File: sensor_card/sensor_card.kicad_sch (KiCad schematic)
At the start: 9 parts, among them J1 Raspberry_Pi_4, J2 BME280, J3 GPS, J4 MPU, J5 parachute, J6 hmi, J7 power, U1 Ai-Thinker-Ra-02

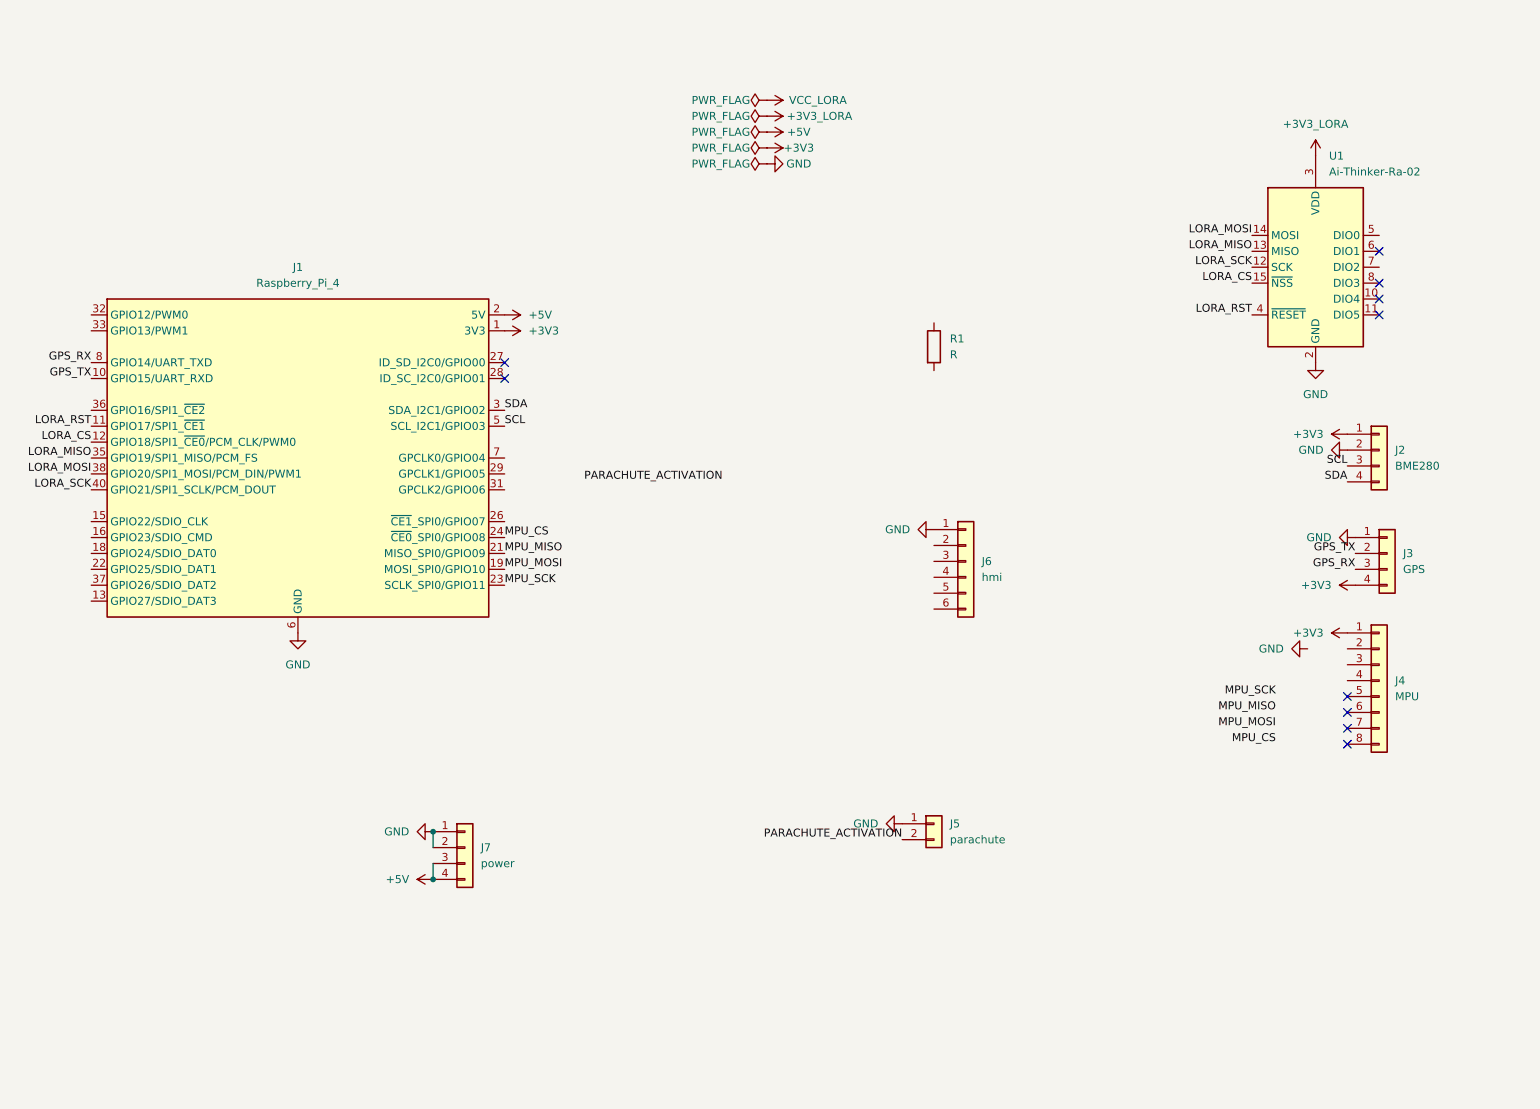
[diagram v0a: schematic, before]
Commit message: Sensor Board Fully Connected
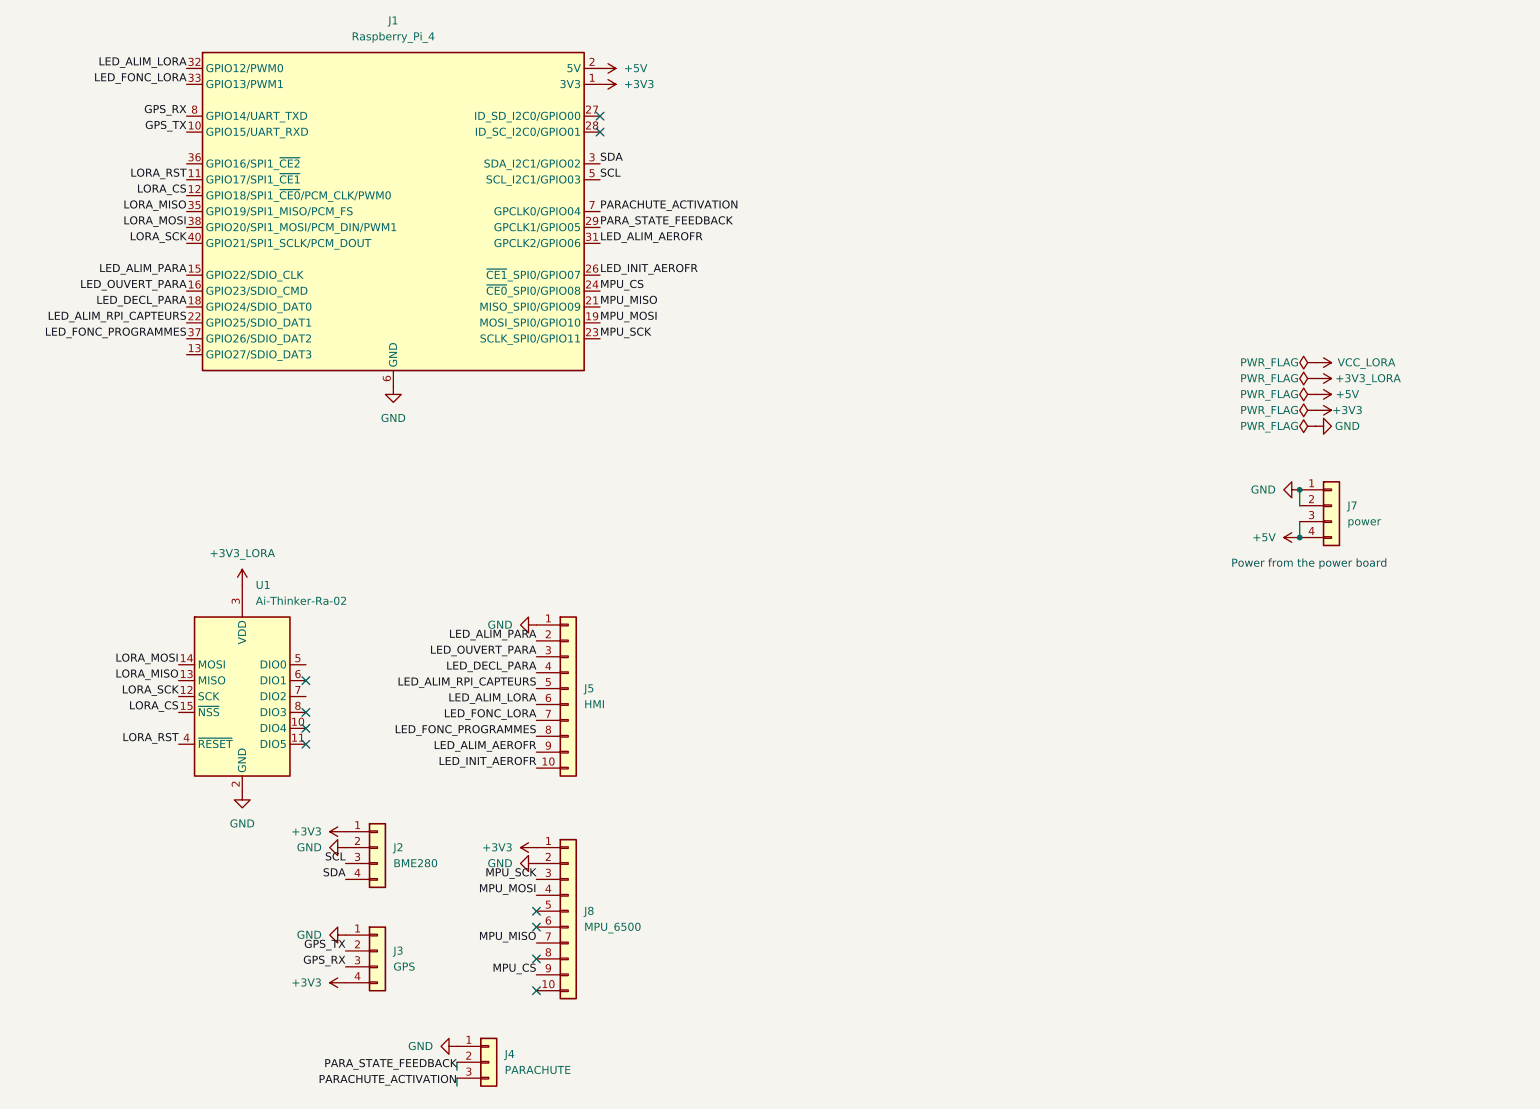
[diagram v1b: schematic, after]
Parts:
- removed J4: MPU, symbol Connector_Generic:Conn_01x08
- removed J5: parachute, symbol Connector_Generic:Conn_01x02
- removed J6: hmi, symbol Connector_Generic:Conn_01x06
- removed R1: R, symbol Device:R
- added J4: PARACHUTE, symbol Connector_Generic:Conn_01x03
- added J5: HMI, symbol Connector_Generic:Conn_01x10
- added J8: MPU_6500, symbol Connector_Generic:Conn_01x10
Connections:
- net +3V3: now also J8.1 (Pin_1)
- net GND: now also J4.1 (Pin_1), J5.1 (Pin_1), J8.2 (Pin_2)
- net MPU_CS: now also J8.9 (Pin_9)
- net MPU_MISO: now also J8.7 (Pin_7)
- net MPU_MOSI: now also J8.4 (Pin_4)
- net MPU_SCK: now also J8.3 (Pin_3)
- net PARACHUTE_ACTIVATION: now also J1.7 (GPCLK0/GPIO04), J4.3 (Pin_3)
- net LED_ALIM_PARA: now reaches J1.15 (GPIO22/SDIO_CLK)
- net LED_ALIM_PARA: now also J5.2 (Pin_2)
- net LED_OUVERT_PARA: now reaches J1.16 (GPIO23/SDIO_CMD)
- net LED_OUVERT_PARA: now also J5.3 (Pin_3)
- net LED_DECL_PARA: now reaches J1.18 (GPIO24/SDIO_DAT0)
- net LED_DECL_PARA: now also J5.4 (Pin_4)
- net LED_ALIM_RPI_CAPTEURS: now reaches J1.22 (GPIO25/SDIO_DAT1)
- net LED_ALIM_RPI_CAPTEURS: now also J5.5 (Pin_5)
- net LED_INIT_AEROFR: now reaches J1.26 (~{CE1}_SPI0/GPIO07)
- net LED_INIT_AEROFR: now also J5.10 (Pin_10)
- net PARA_STATE_FEEDBACK: now reaches J1.29 (GPCLK1/GPIO05)
- net PARA_STATE_FEEDBACK: now also J4.2 (Pin_2)
- net LED_ALIM_AEROFR: now reaches J1.31 (GPCLK2/GPIO06)
- net LED_ALIM_AEROFR: now also J5.9 (Pin_9)
- net LED_ALIM_LORA: now reaches J1.32 (GPIO12/PWM0)
- net LED_ALIM_LORA: now also J5.6 (Pin_6)
- net LED_FONC_LORA: now reaches J1.33 (GPIO13/PWM1)
- net LED_FONC_LORA: now also J5.7 (Pin_7)
- net LED_FONC_PROGRAMMES: now reaches J1.37 (GPIO26/SDIO_DAT2)
- net LED_FONC_PROGRAMMES: now also J5.8 (Pin_8)
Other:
- note added: "Power from the power board"
- moved on the sheet: J1, J2, J3, J7, U1

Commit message: Updated Sensor PCB
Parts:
- added J6: power LORA, Connector_JST:JST_XH_S4B-XH-A-1_1x04_P2.50mm_Horizontal, symbol Connector_Generic:Conn_01x04
- J1: footprint (none) -> Connector_PinHeader_2.54mm:PinHeader_2x20_P2.54mm_Vertical
- J2, J3: footprint (none) -> Connector_PinHeader_2.54mm:PinHeader_1x04_P2.54mm_Vertical
- J4: footprint (none) -> Connector_JST:JST_XH_S3B-XH-A_1x03_P2.50mm_Horizontal
- J5: footprint (none) -> Connector_JST:JST_XH_B10B-XH-A_1x10_P2.50mm_Vertical
- J7: value power -> power_RPI; footprint (none) -> Connector_JST:JST_XH_S4B-XH-A-1_1x04_P2.50mm_Horizontal
- J8: footprint (none) -> Connector_PinHeader_2.54mm:PinHeader_1x10_P2.54mm_Vertical
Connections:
- net +3V3_LORA: now also J6.3 (Pin_3), J6.4 (Pin_4)
- net GND: now also J6.1 (Pin_1), J6.2 (Pin_2)
- no-connect marks 10 -> 14
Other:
- note added: "Power for the LORA"
- note added: "Power from the power board for powering up the RPI"
- note removed: "Power from the power board"
- moved on the sheet: J7

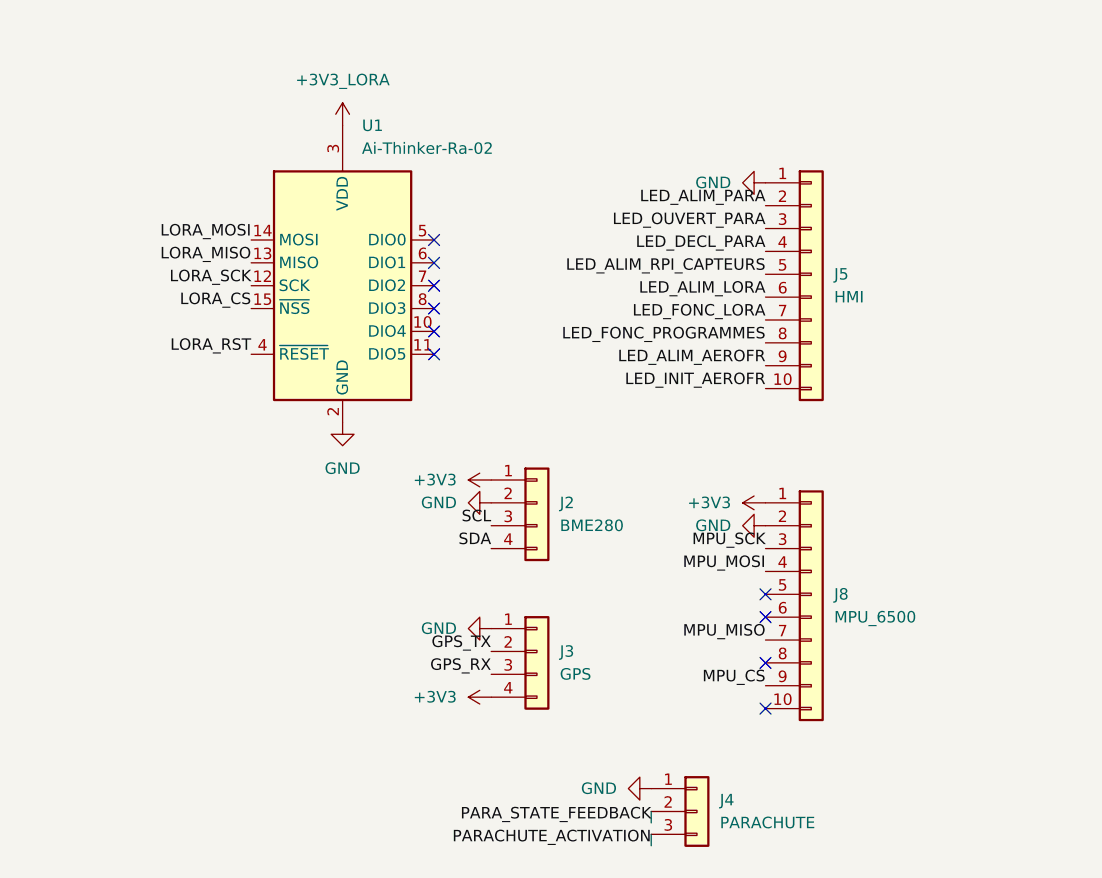
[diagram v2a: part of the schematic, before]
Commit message: Board Routed Prototype 1 .  Power Routes to be redone
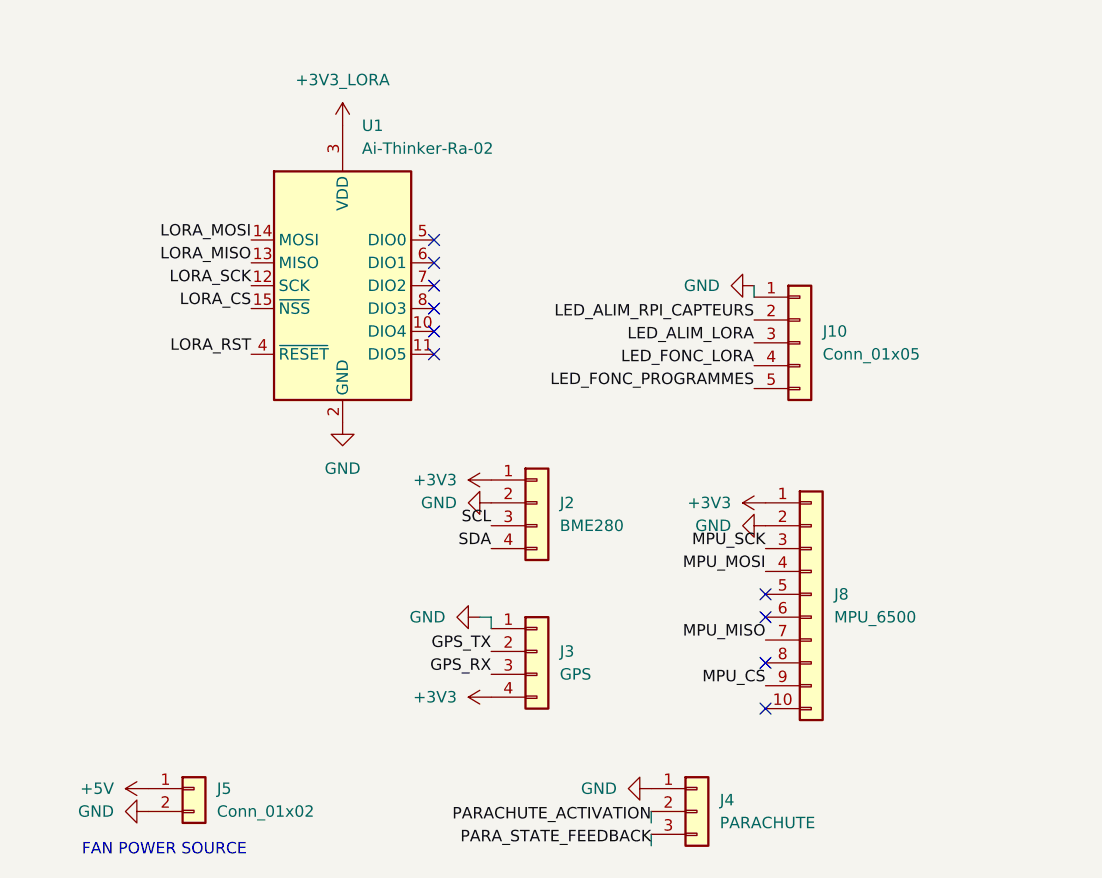
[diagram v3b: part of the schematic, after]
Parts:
- removed J5: HMI, Connector_JST:JST_XH_B10B-XH-A_1x10_P2.50mm_Vertical, symbol Connector_Generic:Conn_01x10
- added J10: Conn_01x05, Connector_JST:JST_XH_S5B-XH-A-1_1x05_P2.50mm_Horizontal, symbol Connector_Generic:Conn_01x05
- added J5: Conn_01x02, Connector_JST:JST_XH_S2B-XH-A_1x02_P2.50mm_Horizontal, symbol Connector_Generic:Conn_01x02
- J2: footprint Connector_PinHeader_2.54mm:PinHeader_1x04_P2.54mm_Vertical -> PHOENIX:BME 280
- J3: footprint Connector_PinHeader_2.54mm:PinHeader_1x04_P2.54mm_Vertical -> PHOENIX:GPS-MV2
- J8: footprint Connector_PinHeader_2.54mm:PinHeader_1x10_P2.54mm_Vertical -> PHOENIX:MPU-9250
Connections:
- net +5V: now also J5.1 (Pin_1)
- net GND: now also J10.1 (Pin_1), J5.2 (Pin_2)
- net LED_ALIM_LORA: now also J10.3 (Pin_3)
- net LED_ALIM_RPI_CAPTEURS: now also J10.2 (Pin_2)
- net LED_FONC_LORA: now also J10.4 (Pin_4)
- net LED_FONC_PROGRAMMES: now also J10.5 (Pin_5)
- net PARACHUTE_ACTIVATION: now also J4.2 (Pin_2); no longer J4.3 (Pin_3)
- net PARA_STATE_FEEDBACK: now also J4.3 (Pin_3); no longer J4.2 (Pin_2)
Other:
- note added: "FAN POWER SOURCE"

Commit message: Fully Routed Sensor board
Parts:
- added H1, H6, H7, H8: MountingHole_RPI, MountingHole:MountingHole_2.2mm_M2_DIN965_Pad, symbol Mechanical:MountingHole_Pad
- added H2, H3, H4, H5: MountingHole_Pad, MountingHole:MountingHole_3.2mm_M3_DIN965_Pad, symbol Mechanical:MountingHole_Pad
- J1: footprint Connector_PinHeader_2.54mm:PinHeader_2x20_P2.54mm_Vertical -> Connector_PinSocket_2.54mm:PinSocket_2x20_P2.54mm_Vertical
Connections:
- net GND: now also H1.1, H2.1, H3.1, H4.1, H5.1, H6.1, H7.1, H8.1
- net LED_ALIM_PARA: no longer names the net of J1.15 (GPIO22/SDIO_CLK)
- net LED_DECL_PARA: no longer names the net of J1.18 (GPIO24/SDIO_DAT0)
- net LED_OUVERT_PARA: no longer names the net of J1.16 (GPIO23/SDIO_CMD)
- no-connect marks 14 -> 17

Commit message: flipped connections for the GPS connector to 3_3,RX <-> GND,TX
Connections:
- net +3V3: now also J3.1 (Pin_1); no longer J3.4 (Pin_4)
- net GND: now also J3.4 (Pin_4); no longer J3.1 (Pin_1)
- net GPS_RX: now also J3.2 (Pin_2); no longer J3.3 (Pin_3)
- net GPS_TX: now also J3.3 (Pin_3); no longer J3.2 (Pin_2)
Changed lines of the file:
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@@
 	)
 	(label "GPS_TX"
+		(at 73.66 170.18 180)
+		(effects
+			(font
+				(size 1.27 1.27)
+			)
+			(justify right bottom)
+		)
+	)
+	(label "GPS_TX"
 		(at 48.26 36.83 180)
 		(effects
@@
 		)
 	)
-	(label "LORA_MISO"
-		(at 46.99 124.46 180)
+	(label "GPS_RX"
+		(at 73.66 167.64 180)
 		(effects
 			(font
@@
 		)
 	)
-	(label "MPU_MISO"
-		(at 104.14 166.37 180)
+	(label "LORA_MISO"
+		(at 46.99 124.46 180)
 		(effects
 			(font
@@
 		)
 	)
-	(label "GPS_TX"
-		(at 73.66 167.64 180)
+	(label "MPU_MISO"
+		(at 104.14 166.37 180)
 		(effects
 			(font
@@
 		)
 	)
-	(label "GPS_RX"
-		(at 73.66 170.18 180)
-		(effects
-			(font
-				(size 1.27 1.27)
-			)
-			(justify right bottom)
-		)
-	)
 	(label "LORA_SCK"
 		(at 46.99 127 180)
@@
 	)
 	(symbol
-		(lib_id "power:+3V3")
-		(at 73.66 172.72 90)
-		(unit 1)
-		(exclude_from_sim no)
-		(in_bom yes)
-		(on_board yes)
-		(dnp no)
-		(fields_autoplaced yes)
-		(property "Reference" "#PWR09"
-			(at 77.47 172.72 0)
-			(effects
-				(font
-					(size 1.27 1.27)
-				)
-				(hide yes)
-			)
-		)
-		(property "Value" "+3V3"
-			(at 69.85 172.7199 90)
-			(effects
-				(font
-					(size 1.27 1.27)
-				)
-				(justify left)
-			)
-		)
-		(property "Footprint" ""
-			(at 73.66 172.72 0)
-			(effects
-				(font
-					(size 1.27 1.27)
-				)
-				(hide yes)
-			)
-		)
-		(property "Datasheet" ""
-			(at 73.66 172.72 0)
-			(effects
-				(font
-					(size 1.27 1.27)
-				)
-				(hide yes)
-			)
-		)
-		(property "Description" "Power symbol creates a global label with name \"+3V3\""
-			(at 73.66 172.72 0)
-			(effects
-				(font
-					(size 1.27 1.27)
-				)
-				(hide yes)
-			)
-		)
-		(pin "1"
-		)
-		(instances
-			(project "sensor_card"
-				(path "/acfc41ca-ba25-42c0-b943-b6d367d2bef8"
-					(reference "#PWR09")
-					(unit 1)
-				)
-			)
-		)
-	)
-	(symbol
 		(lib_id "Connector_Generic:Conn_01x04")
 		(at 78.74 167.64 0)
@@
 	)
 	(symbol
-		(lib_id "power:GND")
-		(at 72.39 163.83 270)
-		(unit 1)
-		(exclude_from_sim no)
-		(in_bom yes)
-		(on_board yes)
-		(dnp no)
-		(fields_autoplaced yes)
-		(property "Reference" "#PWR017"
-			(at 66.04 163.83 0)
-			(effects
-				(font
-					(size 1.27 1.27)
-				)
-				(hide yes)
-			)
-		)
-		(property "Value" "GND"
-			(at 68.58 163.8299 90)
-			(effects
-				(font
-					(size 1.27 1.27)
-				)
-				(justify right)
-			)
-		)
-		(property "Footprint" ""
-			(at 72.39 163.83 0)
-			(effects
-				(font
-					(size 1.27 1.27)
-				)
-				(hide yes)
-			)
-		)
-		(property "Datasheet" ""
-			(at 72.39 163.83 0)
-			(effects
-				(font
-					(size 1.27 1.27)
-				)
-				(hide yes)
-			)
-		)
-		(property "Description" "Power symbol creates a global label with name \"GND\" , ground"
-			(at 72.39 163.83 0)
-			(effects
-				(font
-					(size 1.27 1.27)
-				)
-				(hide yes)
-			)
-		)
-		(pin "1"
-		)
-		(instances
-			(project "sensor_card"
-				(path "/acfc41ca-ba25-42c0-b943-b6d367d2bef8"
-					(reference "#PWR017")
-					(unit 1)
-				)
-			)
-		)
-	)
-	(symbol
 		(lib_id "Connector:Raspberry_Pi_4")
 		(at 81.28 49.53 0)
@@
 	)
 	(symbol
+		(lib_id "power:+3V3")
+		(at 72.39 163.83 90)
+		(unit 1)
+		(exclude_from_sim no)
+		(in_bom yes)
+		(on_board yes)
+		(dnp no)
+		(fields_autoplaced yes)
+		(property "Reference" "#PWR017"
+			(at 76.2 163.83 0)
+			(effects
+				(font
+					(size 1.27 1.27)
+				)
+				(hide yes)
+			)
+		)
+		(property "Value" "+3V3"
+			(at 68.58 163.8299 90)
+			(effects
+				(font
+					(size 1.27 1.27)
+				)
+				(justify left)
+			)
+		)
+		(property "Footprint" ""
+			(at 72.39 163.83 0)
+			(effects
+				(font
+					(size 1.27 1.27)
+				)
+				(hide yes)
+			)
+		)
+		(property "Datasheet" ""
+			(at 72.39 163.83 0)
+			(effects
+				(font
+					(size 1.27 1.27)
+				)
+				(hide yes)
+			)
+		)
+		(property "Description" "Power symbol creates a global label with name \"+3V3\""
+			(at 72.39 163.83 0)
+			(effects
+				(font
+					(size 1.27 1.27)
+				)
+				(hide yes)
+			)
+		)
+		(pin "1"
+		)
+		(instances
+			(project "sensor_card"
+				(path "/acfc41ca-ba25-42c0-b943-b6d367d2bef8"
+					(reference "#PWR017")
+					(unit 1)
+				)
+			)
+		)
+	)
+	(symbol
 		(lib_id "Connector_Generic:Conn_01x04")
 		(at 78.74 151.13 0)
@@
 					(unit 1)
 				)
+			)
+		)
+	)
+	(symbol
+		(lib_id "power:GND")
+		(at 73.66 172.72 270)
+		(unit 1)
+		(exclude_from_sim no)
+		(in_bom yes)
+		(on_board yes)
+		(dnp no)
+		(fields_autoplaced yes)
+		(property "Reference" "#PWR026"
+			(at 67.31 172.72 0)
+			(effects
+				(font
+					(size 1.27 1.27)
+				)
+				(hide yes)
+			)
+		)
+		(property "Value" "GND"
+			(at 69.85 172.7199 90)
+			(effects
+				(font
+					(size 1.27 1.27)
+				)
+				(justify right)
+			)
+		)
+		(property "Footprint" ""
+			(at 73.66 172.72 0)
+			(effects
+				(font
+					(size 1.27 1.27)
+				)
+				(hide yes)
+			)
+		)
+		(property "Datasheet" ""
+			(at 73.66 172.72 0)
+			(effects
+				(font
+					(size 1.27 1.27)
+				)
+				(hide yes)
+			)
+		)
+		(property "Description" "Power symbol creates a global label with name \"GND\" , ground"
+			(at 73.66 172.72 0)
+			(effects
+				(font
+					(size 1.27 1.27)
+				)
+				(hide yes)
+			)
+		)
+		(pin "1"
+		)
+		(instances
+			(project "sensor_card"
+				(path "/acfc41ca-ba25-42c0-b943-b6d367d2bef8"
+					(reference "#PWR026")
+					(unit 1)
+				)
